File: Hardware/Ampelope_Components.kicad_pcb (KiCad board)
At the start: 2 copper layers, 60.5 x 81.6 mm, 101 parts, among them J1 Conn_01x12_Male, J18 SWD_Header, J19 USB_B_Micro, J2 Conn_01x12_Male, J3 Conn_01x12_Male, J4 Conn_01x12_Male, J5 Eurorack_16_pin_power, Q1 MMBT3904, Q2 MMBT3904, Q3 MMBT3904, Q4 MMBT3904, Q5 MMBT3904, U1 STM32G431RB, U2 AS3364, U3 LM1117-3.3, U4 TL074, U5 TL074, U6 TL074, Y1 8MHz 20pF

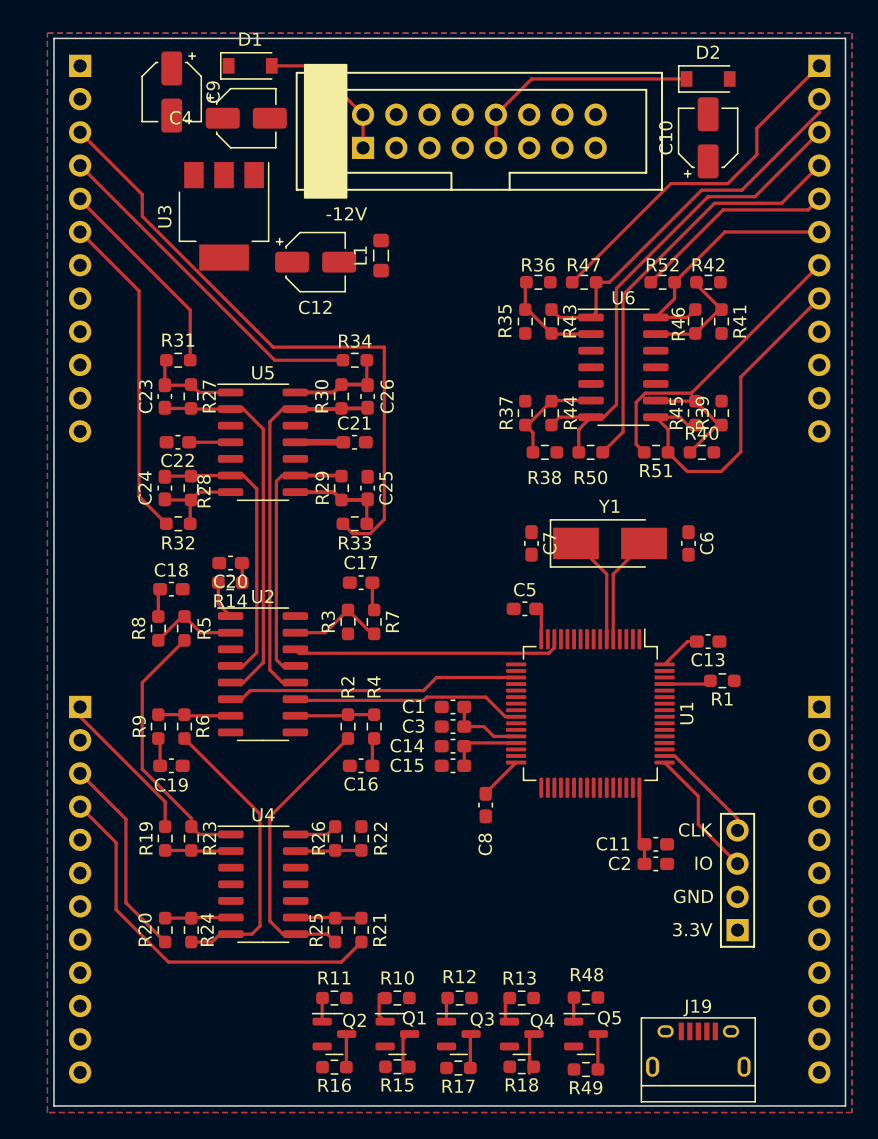
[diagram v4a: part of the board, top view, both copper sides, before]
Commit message: Draft of panel layout
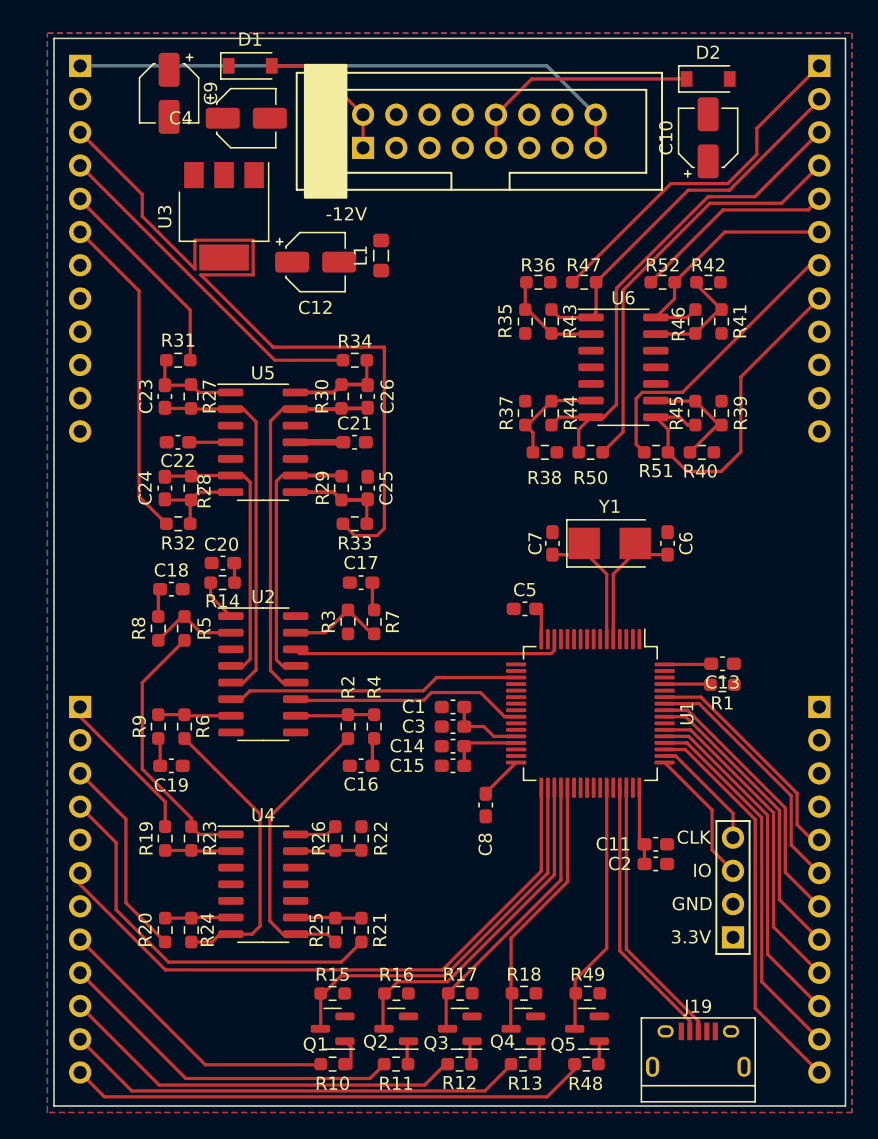
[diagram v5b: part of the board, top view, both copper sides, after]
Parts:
- moved R15 7.47 mm to (81.3, 98.4), turned to 0 degrees
- moved R16 7.36 mm to (86.2, 98.4), turned to 0 degrees
- moved R10 7.07 mm to (81.3, 103.8), turned to 0 degrees
- moved R11 6.91 mm to (86.2, 103.8), turned to 0 degrees
- moved R49 5.83 mm to (100.8, 98.4), turned to 0 degrees
- moved R17 5.71 mm to (91.0, 98.4), turned to 0 degrees
- moved R18 5.62 mm to (95.9, 98.4), turned to 0 degrees
- moved R48 5.09 mm to (100.7, 103.8), turned to 0 degrees
- moved R13 5.05 mm to (95.8, 103.8), turned to 0 degrees
- moved R12 5.05 mm to (91.0, 103.8), turned to 0 degrees
- moved Q1 4.97 mm to (81.3, 101.1), turned to 180 degrees
- moved Q2 4.74 mm to (86.2, 101.1), turned to 180 degrees
- moved C13 2.02 mm to (111.1, 73.2)
- moved C6 1.60 mm to (106.9, 64.0)
- moved C7 1.60 mm to (98.1, 64.0)
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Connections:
- J1 pad 1: unconnected-(J1-Pad1) -> /Gate_In
- J2 pad 10: /Env4_LFO -> /Gate3_In
- J2 pad 11: /Env1_LFO -> /Gate4_In
- J2 pad 12: unconnected-(J2-Pad12) -> /Clock_In
- J2 pad 5: /Clock_In -> unconnected-(J2-Pad5)
- J2 pad 7: /Env3_Short -> unconnected-(J2-Pad7)
- J2 pad 8: /Env3_LFO -> /Gate1_In
- J2 pad 9: /Env4_Short -> /Gate2_In
- J4 pad 10: /Gate4_In -> /Env4_Short
- J4 pad 11: unconnected-(J4-Pad11) -> /Env3_LFO
- J4 pad 12: unconnected-(J4-Pad12) -> /Env3_Short
- J4 pad 5: /Env2_Short -> /Env2_LFO
- J4 pad 6: /Env2_LFO -> /Env2_Short
- J4 pad 7: /Gate1_In -> /Env1_LFO
- J4 pad 8: /Gate2_In -> /Env1_Short
- J4 pad 9: /Gate3_In -> /Env4_LFO
- U1 pad 34: /Env3_Short -> /Gate1_Inv
- U1 pad 35: /Env3_LFO -> /Gate2_Inv
- U1 pad 36: /Env4_Short -> /Gate3_Inv
- U1 pad 37: /Env4_LFO -> /Gate4_Inv
- U1 pad 38: /Gate1_Inv -> unconnected-(U1-Pad38)
- U1 pad 39: /Gate2_Inv -> unconnected-(U1-Pad39)
- U1 pad 40: /Gate3_Inv -> unconnected-(U1-Pad40)
- U1 pad 41: /Gate4_Inv -> unconnected-(U1-Pad41)
- U1 pad 42: /Env1_Short -> unconnected-(U1-Pad42)
- U1 pad 51: unconnected-(U1-Pad51) -> /Env3_Short
- U1 pad 52: unconnected-(U1-Pad52) -> /Env3_LFO
- U1 pad 53: unconnected-(U1-Pad53) -> /Env4_Short
- U1 pad 54: unconnected-(U1-Pad54) -> /Env4_LFO
- U1 pad 56: /Env1_LFO -> /Env1_Short
- U1 pad 57: /Env2_Short -> /Env1_LFO
- U1 pad 58: /Env2_LFO -> /Env2_Short
- U1 pad 59: unconnected-(U1-Pad59) -> /Env2_LFO
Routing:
- net /LFO_Speed: track 0.00 -> 48.3 mm
- net /Gate_In: track 0.00 -> 43.5 mm
- net /Clock_In: track 0.00 -> 39.8 mm
- net /Gate4_In: track 0.00 -> 35.4 mm
- net /Gate3_In: track 0.00 -> 31.0 mm
- net /Env3_Short: track 0.00 -> 30.5 mm
- net /Env3_LFO: track 0.00 -> 28.6 mm
- net /Gate1_Inv: track 3.22 -> 30.3 mm
- net /Gate2_In: track 0.00 -> 26.9 mm
- net /Env4_Short: track 0.00 -> 26.6 mm
- net /Env4_LFO: track 0.00 -> 24.6 mm
- net /Gate2_Inv: track 2.65 -> 26.2 mm
- net /Env1_Short: track 0.00 -> 22.9 mm
- net /Gate1_In: track 0.00 -> 22.4 mm
- net /Env1_LFO: track 0.00 -> 20.9 mm
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
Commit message: Layout on component board
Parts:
- RESET1: footprint Custom_Footprints:SW_PUSH_6mm_aligned -> Custom_Footprints:SW_SPST_EVQQ2
- moved RESET1 76.8 mm to (116.6, 66.0), turned to 90 degrees
- moved L1 39.4 mm to (90.5, 81.0), turned to 0 degrees
- moved C12 14.0 mm to (66.6, 38.3), turned to -90 degrees
- moved C9 12.2 mm to (77.3, 38.3)
- moved U3 9.18 mm to (69.7, 30.4), turned to 180 degrees
- moved C4 7.32 mm to (72.0, 38.3), turned to -90 degrees
- moved R7 4.73 mm to (81.8, 66.1)
- moved R8 4.41 mm to (68.3, 66.1)
- moved R5 4.41 mm to (70.2, 66.1)
- moved C18 4.31 mm to (69.3, 63.2)
- moved C20 4.20 mm to (72.9, 61.3)
- moved R3 4.09 mm to (83.7, 66.1), turned to 90 degrees
- moved R24 4.07 mm to (70.2, 89.5)
- moved R25 4.07 mm to (81.8, 89.5)
- moved C16 4.06 mm to (82.8, 77.0)
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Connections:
- J1 pad 12: unconnected-(J1-Pad12) -> /Audio1_Out
- J1 pad 3: /Audio4_Out -> unconnected-(J1-Pad3)
- J1 pad 4: /Audio3_Out -> unconnected-(J1-Pad4)
- J1 pad 5: /Audio2_Out -> unconnected-(J1-Pad5)
- J1 pad 6: /Audio1_Out -> unconnected-(J1-Pad6)
- J1 pad 7: unconnected-(J1-Pad7) -> /Audio4_Out
- J1 pad 8: unconnected-(J1-Pad8) -> /Audio3_Out
- J1 pad 9: unconnected-(J1-Pad9) -> /Audio2_Out
- J2 pad 2: /Audio4_In -> unconnected-(J2-Pad2)
- J2 pad 6: /LFO_Speed -> /Audio4_In
- J2 pad 7: unconnected-(J2-Pad7) -> /LFO_Speed
- J3 pad 1: /Led1_Out -> unconnected-(J3-Pad1)
- J3 pad 10: /EnvB_Decay -> /EnvB_Sustain
- J3 pad 11: /EnvB_Sustain -> /EnvB_Decay
- J3 pad 12: /EnvB_Release -> /EnvB_Attack
- J3 pad 2: /Env1_Out -> unconnected-(J3-Pad2)
- J3 pad 3: /Env2_Out -> /Led1_Out
- J3 pad 4: /Led2_Out -> /Env1_Out
- J3 pad 5: /Led4_Out -> /Led2_Out
- J3 pad 6: /Env4_Out -> /Led4_Out
- J3 pad 7: /Led3_Out -> /Env3_Out
- J3 pad 8: /Env3_Out -> /Led3_Out
- J3 pad 9: /EnvB_Attack -> /EnvB_Release
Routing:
- net VCC: track 3.16 -> 113.0 mm, vias 0 -> 5
- net VEE: track 3.66 -> 110.0 mm, vias 0 -> 6
- net /Env1_DAC: track 0.00 -> 55.0 mm, vias 0 -> 2
- net /EnvB_Release: track 0.00 -> 45.2 mm, vias 0 -> 1
- net /EnvB_Sustain: track 0.00 -> 40.9 mm, vias 0 -> 1
- net /Audio4_In: track 0.00 -> 34.7 mm
- net /Env4_DAC: track 20.2 -> 54.9 mm, vias 0 -> 3
- net /EnvB_Decay: track 0.00 -> 34.1 mm, vias 0 -> 1
- net /Env2_Out: track 38.0 -> 5.40 mm
- net /Env3_DAC: track 17.8 -> 50.2 mm, vias 0 -> 3
- net /EnvB_Attack: track 0.00 -> 32.0 mm, vias 0 -> 1
- net /EnvA_Release: track 0.00 -> 25.7 mm, vias 0 -> 1
- net /EnvA_Sustain: track 0.00 -> 23.5 mm, vias 0 -> 1
- net /Audio4_Out: track 61.3 -> 38.2 mm
- net /RESET: track 0.00 -> 22.8 mm
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- added copper zone on In2.Cu, net +3V3
- added copper zone on B.Cu, net GND
- added copper zone on F.Cu, net GND
- added copper zone on In1.Cu, net GND
- removed copper zone on B.Cu, net +3V3
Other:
- copper layers 2 -> 4

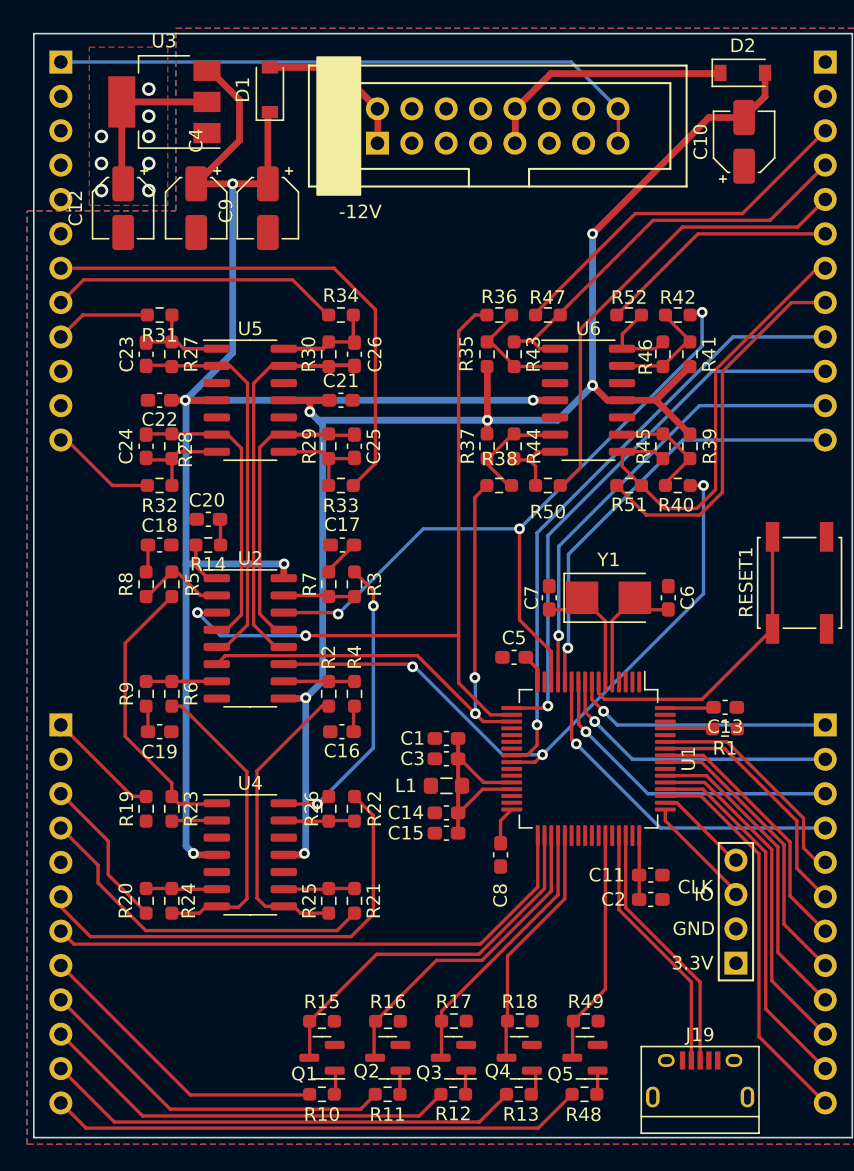
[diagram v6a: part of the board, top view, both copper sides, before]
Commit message: Component layout refinement; pre change of input protection transistors to PNPs
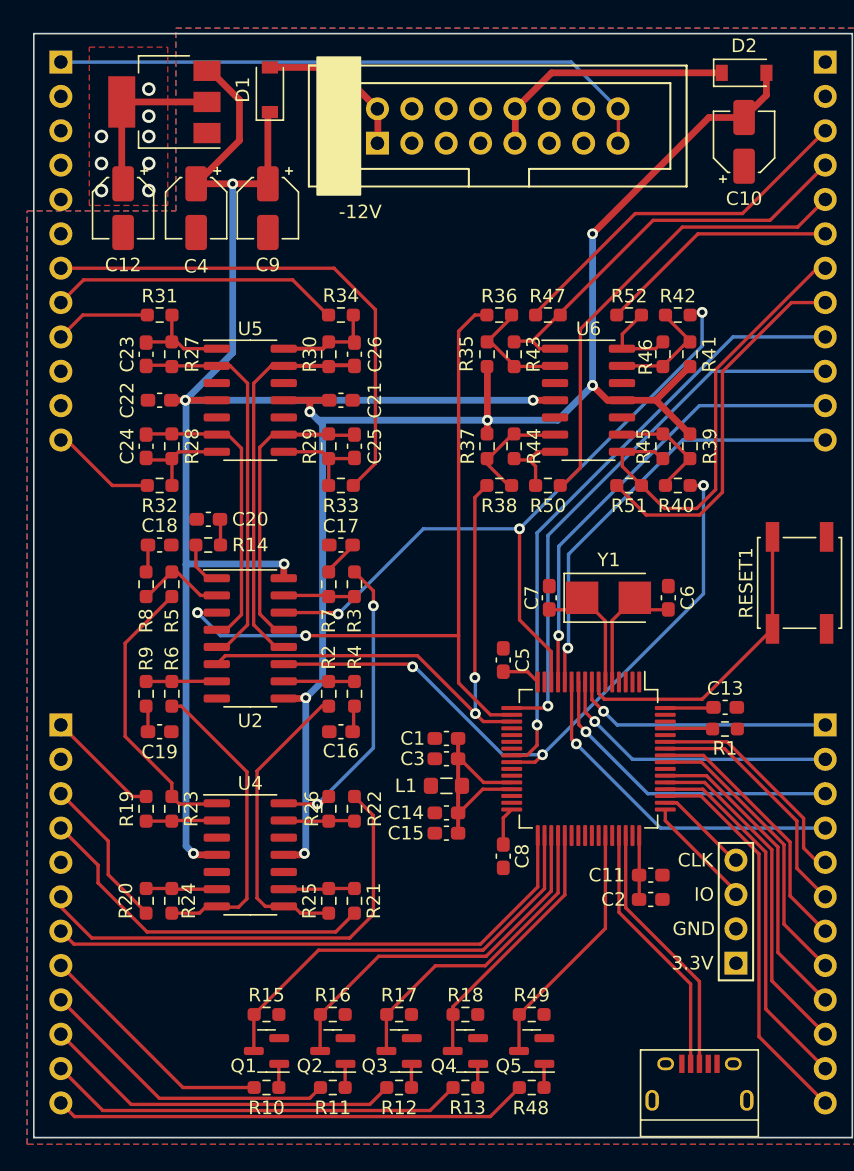
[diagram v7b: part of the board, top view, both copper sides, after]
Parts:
- moved Q1 4.13 mm to (77.2, 100.6)
- moved R10 4.13 mm to (77.2, 103.3)
- moved R15 4.13 mm to (77.2, 97.9)
- moved R16 4.11 mm to (82.1, 97.9)
- moved Q2 4.09 mm to (82.1, 100.6)
- moved R11 4.08 mm to (82.1, 103.3)
- moved R17 4.08 mm to (87.0, 97.9)
- moved R18 4.05 mm to (91.9, 97.9)
- moved Q3 4.05 mm to (87.0, 100.6)
- moved R12 4.03 mm to (87.0, 103.3)
- moved R49 4.03 mm to (96.8, 97.9)
- moved Q4 4.01 mm to (91.9, 100.6)
- moved R13 3.98 mm to (91.9, 103.3)
- moved Q5 3.97 mm to (96.8, 100.6)
- moved R48 3.93 mm to (96.8, 103.3)
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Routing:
- net /Clock_In: track 39.7 -> 35.2 mm
- net /Gate3_In: track 31.3 -> 26.8 mm
- net /Gate4_In: track 35.4 -> 31.0 mm
- net /Gate2_In: track 26.9 -> 22.5 mm
- net /Gate1_In: track 22.4 -> 18.0 mm
- net /Gate1_Inv: track 27.9 -> 32.0 mm
- net /Gate2_Inv: track 23.7 -> 27.7 mm
- net /Gate3_Inv: track 20.0 -> 23.3 mm
- net Net-(R19-Pad1): track 2.95 -> 4.85 mm
- net /Clock_Inv: track 17.2 -> 18.6 mm
- net /Gate4_Inv: track 18.1 -> 19.4 mm
- net /Audio3_In_Buff: track 22.4 -> 21.7 mm
- net +3V3: track 25.2 -> 25.8 mm

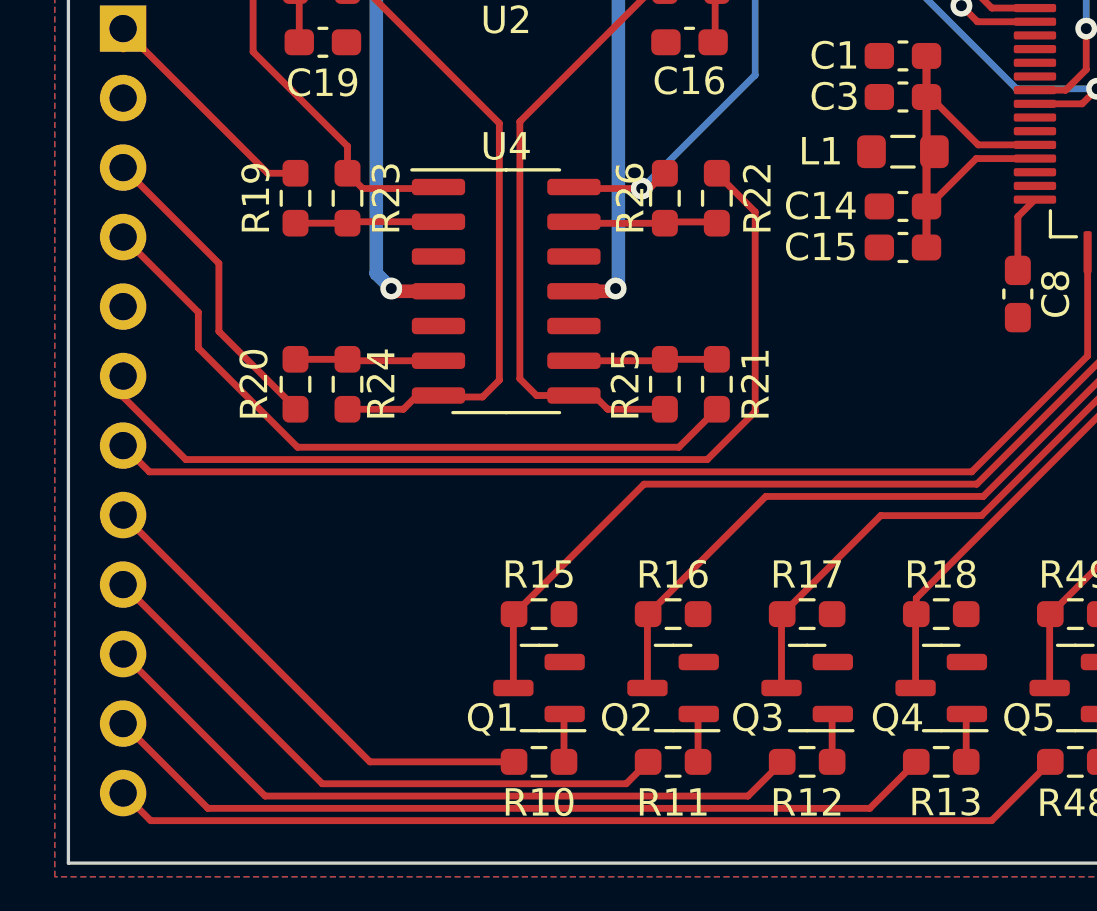
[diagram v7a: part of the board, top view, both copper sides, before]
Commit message: Updated to work correctly with AS3364 (gain levels, non inverting etc)
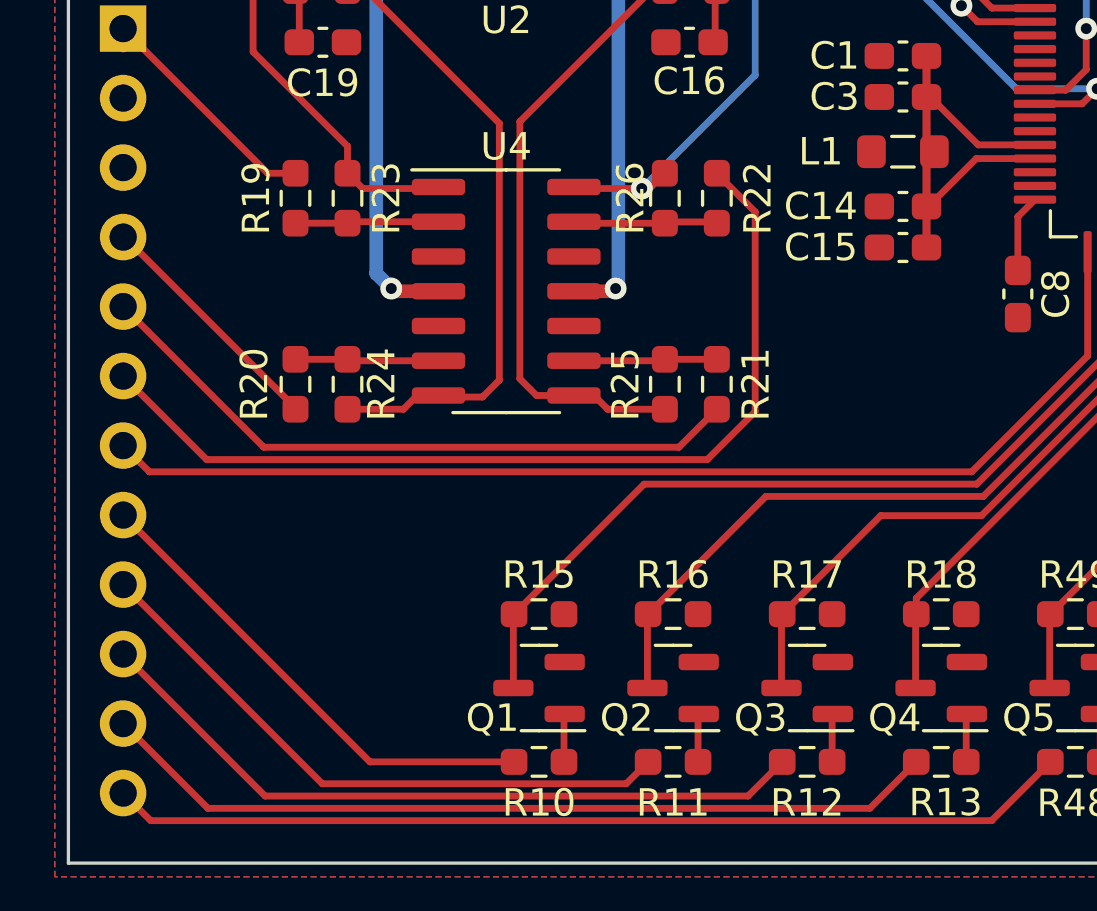
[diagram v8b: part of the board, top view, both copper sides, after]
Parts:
- Q1, Q2, Q3, Q4, Q5: value MMBT3904 -> MMBT3906
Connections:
- J2 pad 3: /Audio2_In -> unconnected-(J2-Pad3)
- J2 pad 4: /Audio3_In -> /Audio2_In
- J2 pad 5: unconnected-(J2-Pad5) -> /Audio3_In
- Q1 pad 2: GND -> +3V3
- Q2 pad 2: GND -> +3V3
- Q3 pad 2: GND -> +3V3
- Q4 pad 2: GND -> +3V3
- Q5 pad 2: GND -> +3V3
- R15 pad 2: +3V3 -> GND
- R16 pad 2: +3V3 -> GND
- R17 pad 2: +3V3 -> GND
- R18 pad 2: +3V3 -> GND
- R49 pad 2: +3V3 -> GND
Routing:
- net /Audio2_In: track 11.7 -> 9.17 mm
- net /Audio3_In: track 26.2 -> 24.4 mm
